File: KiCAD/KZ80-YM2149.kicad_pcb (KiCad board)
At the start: 2 copper layers, 100 x 74 mm, 27 parts, among them J1 ADDR JP, J2 Conn_01x02, J3 SBC8080 BUS, U1 74HC00, U2 74HC138, U3 74HC02, U4 74HC74, U5 YM2149, Y1 3.57MHz

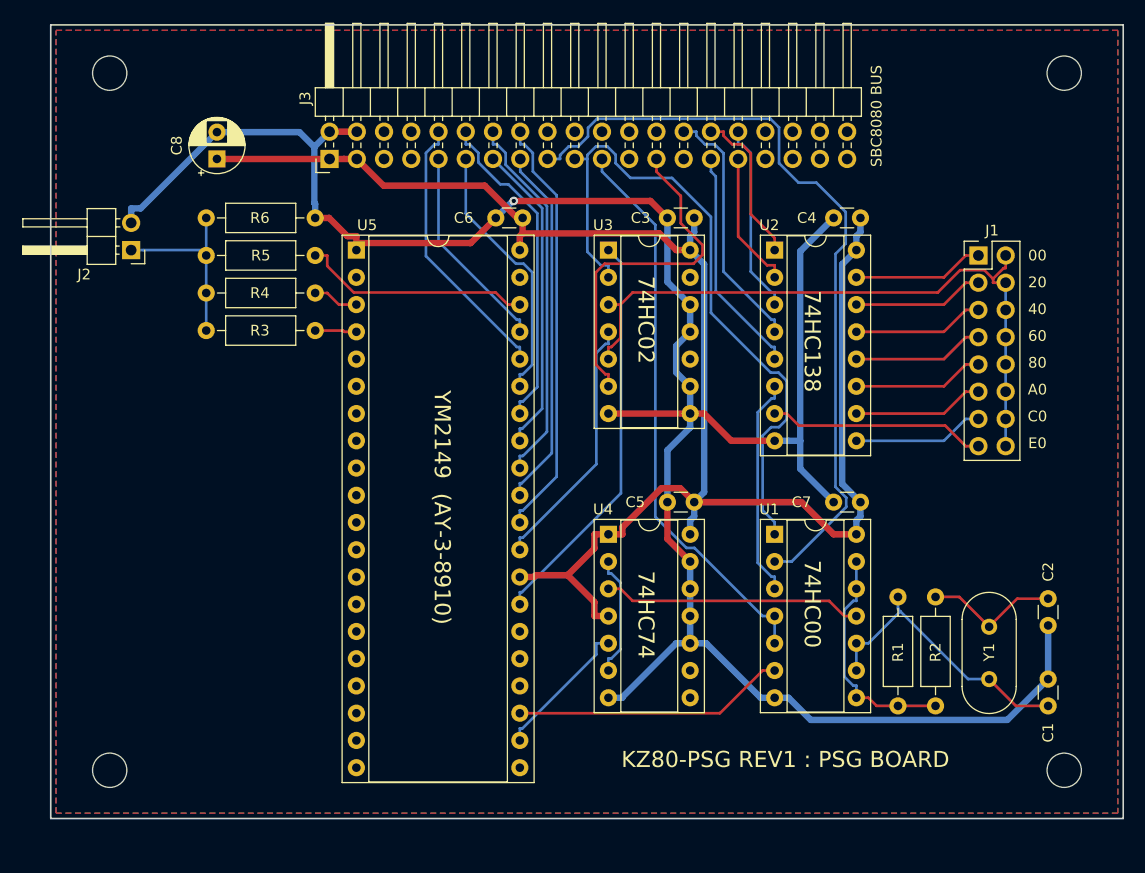
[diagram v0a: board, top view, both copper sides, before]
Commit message: ジョイスティックポート接続&プリントパターン見直し
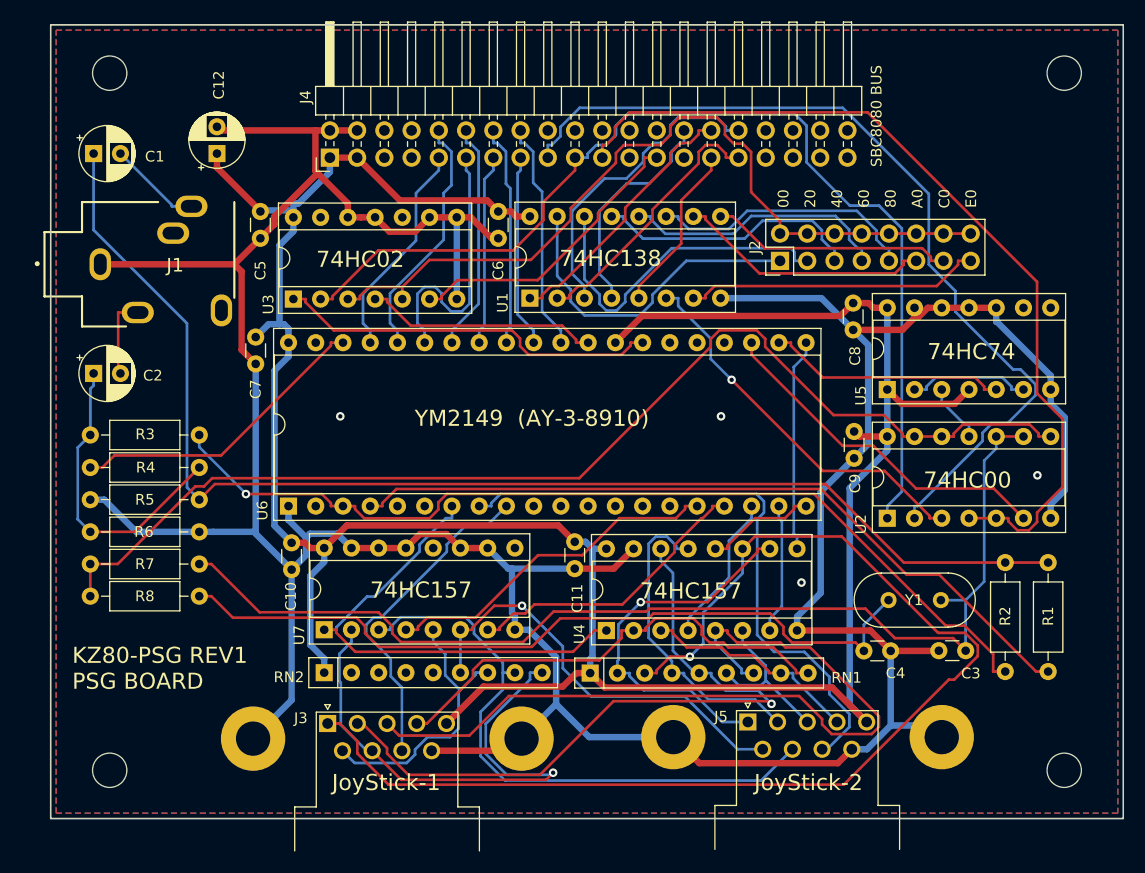
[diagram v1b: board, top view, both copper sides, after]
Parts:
- added C10: 0.1u, Capacitor_THT:C_Disc_D3.0mm_W1.6mm_P2.50mm, F.Cu at (112.5, 98.3)
- added C11: 0.1u, Capacitor_THT:C_Disc_D3.0mm_W1.6mm_P2.50mm, F.Cu at (138.9, 98.2)
- added C12: 10u, Capacitor_THT:CP_Radial_D5.0mm_P2.50mm, F.Cu at (105.5, 62.0)
- added C9: 0.1u, Capacitor_THT:C_Disc_D3.0mm_W1.6mm_P2.50mm, F.Cu at (164.9, 87.9)
- added J4: SBC8080 BUS, Connector_PinHeader_2.54mm:PinHeader_2x20_P2.54mm_Horizontal, F.Cu at (116.0, 62.4)
- added J5: JOYSTICK2, DSUB:DSUB-9_Male_Horizontal_P2.77x2.54mm_EdgePinOffset9.40mm, F.Cu at (155.0, 115.0)
- added R7: 1M, Resistor_THT:R_Axial_DIN0207_L6.3mm_D2.5mm_P10.16mm_Horizontal, F.Cu at (93.7, 100.3)
- added R8: 1k, Resistor_THT:R_Axial_DIN0207_L6.3mm_D2.5mm_P10.16mm_Horizontal, F.Cu at (93.7, 103.3)
- added RN1: 10k, Resistor_THT:R_Array_SIP9, F.Cu at (140.3, 110.4)
- added RN2: 10k, Resistor_THT:R_Array_SIP9, F.Cu at (115.5, 110.4)
- added U6: YM2149, Package_DIP:DIP-40_W15.24mm_Socket, F.Cu at (112.2, 94.9)
- added U7: 74HC157, Package_DIP:DIP-16_W7.62mm_Socket, F.Cu at (115.5, 106.4)
- C1, C2: value 22p -> 1u; footprint Capacitor_THT:C_Disc_D3.0mm_W1.6mm_P2.50mm -> Capacitor_THT:CP_Radial_D5.0mm_P2.50mm
- C3, C4: value 0.1u -> 22p
- C8: value 10u -> 0.1u; footprint Capacitor_THT:CP_Radial_D5.0mm_P2.50mm -> Capacitor_THT:C_Disc_D3.0mm_W1.6mm_P2.50mm
- J1: value ADDR JP -> Audio-Jack-3_2Switches; footprint Connector_PinHeader_2.54mm:PinHeader_2x08_P2.54mm_Vertical -> AJ-1780:AJ-1780
- J2: value Conn_01x02 -> ADDR JP; footprint Connector_PinHeader_2.54mm:PinHeader_1x02_P2.54mm_Horizontal -> Connector_PinHeader_2.54mm:PinHeader_2x08_P2.54mm_Vertical
- J3: value SBC8080 BUS -> JOYSTICK1; footprint Connector_PinHeader_2.54mm:PinHeader_2x20_P2.54mm_Horizontal -> DSUB:DSUB-9_Male_Horizontal_P2.77x2.54mm_EdgePinOffset9.40mm
- R1: value 1M -> 1k
- R2, R3, R5: value 1k -> 2.2k
- R6: value 2k -> 2.2k
- U1: value 74HC00 -> 74HC138; footprint Package_DIP:DIP-14_W7.62mm_Socket -> Package_DIP:DIP-16_W7.62mm_Socket
- U2: value 74HC138 -> 74HC00; footprint Package_DIP:DIP-16_W7.62mm_Socket -> Package_DIP:DIP-14_W7.62mm_Socket
- U4: value 74HC74 -> 74HC157; footprint Package_DIP:DIP-14_W7.62mm_Socket -> Package_DIP:DIP-16_W7.62mm_Socket
- U5: value YM2149 -> 74HC74; footprint Package_DIP:DIP-40_W15.24mm_Socket -> Package_DIP:DIP-14_W7.62mm_Socket
- moved C1 102.8 mm to (94.0, 62.0), turned to 0 degrees
- moved C2 91.4 mm to (94.0, 82.5), turned to 0 degrees
- moved J1 83.6 mm to (92.9, 72.3)
- moved C8 60.8 mm to (164.8, 75.9), turned to 270 degrees
- moved J2 60.5 mm to (158.0, 72.0), turned to 90 degrees
- moved C7 58.5 mm to (109.1, 79.1), turned to 270 degrees
- moved J3 52.6 mm to (115.8, 115.1), turned to 0 degrees
- moved U5 51.2 mm to (168.0, 84.0), turned to 90 degrees
- moved C5 48.7 mm to (109.5, 67.4), turned to 270 degrees
- moved C3 47.6 mm to (175.3, 108.3)
- moved C4 40.4 mm to (165.8, 108.4), turned to 0 degrees
- moved U1 31.7 mm to (134.7, 75.5), turned to 90 degrees
- moved R6 31.2 mm to (93.7, 97.3)
- moved U3 29.7 mm to (112.6, 75.6), turned to 90 degrees
- moved U2 27.1 mm to (168.0, 96.0), turned to 90 degrees
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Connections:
- C1 pad 2: GND -> Net-(C1-Pad2)
- C2 pad 2: GND -> Net-(C2-Pad2)
- C3 pad 1: VCC -> Net-(C3-Pad1)
- C4 pad 1: VCC -> Net-(C4-Pad1)
- J1 pad 1: Net-(J1-Pad1) -> GND
- J1 pad 2: Net-(J1-Pad10) -> Net-(C1-Pad2)
- J1 pad 3: Net-(J1-Pad3) -> (no net)
- J1 pad 4: Net-(J1-Pad10) -> (no net)
- J1 pad 5: Net-(J1-Pad5) -> Net-(C2-Pad2)
- J2 pad 2: GND -> Net-(J2-Pad10)
- J3 pad 1: VCC -> Net-(J3-Pad1)
- J3 pad 2: GND -> Net-(J3-Pad2)
- J3 pad 3: VCC -> Net-(J3-Pad3)
- J3 pad 4: GND -> Net-(J3-Pad4)
- J3 pad 5: Net-(J3-Pad5) -> VCC
- J3 pad 9: D0 -> GND
- R1 pad 1: Net-(R1-Pad1) -> Net-(C1-Pad1)
- R1 pad 2: Net-(C1-Pad1) -> Net-(R1-Pad2)
- R2 pad 1: Net-(R1-Pad1) -> Net-(C1-Pad1)
- R2 pad 2: Net-(C2-Pad1) -> Net-(R2-Pad2)
- R3 pad 1: Net-(J2-Pad1) -> Net-(C2-Pad1)
- R3 pad 2: Net-(R3-Pad2) -> Net-(R2-Pad2)
- R4 pad 1: Net-(J2-Pad1) -> Net-(C2-Pad1)
- R5 pad 1: Net-(J2-Pad1) -> Net-(C1-Pad1)
- R5 pad 2: Net-(R5-Pad2) -> GND
- R6 pad 1: Net-(J2-Pad1) -> Net-(C2-Pad1)
- U1 pad 1: /~IOWR -> /A5
- U1 pad 10: Net-(C1-Pad1) -> Net-(J2-Pad11)
- U1 pad 11: Net-(U1-Pad11) -> Net-(J2-Pad9)
- U1 pad 12: Net-(R1-Pad1) -> Net-(J2-Pad7)
- U1 pad 13: Net-(R1-Pad1) -> Net-(J2-Pad5)
- U1 pad 14: VCC -> Net-(J2-Pad3)
- U1 pad 2: /~IORD -> /A6
- U1 pad 3: Net-(U1-Pad3) -> /A7
- U1 pad 4: /RES -> /A3
- U1 pad 5: /RES -> /A4
- U1 pad 7: GND -> Net-(J2-Pad15)
- U1 pad 8: Net-(R1-Pad1) -> GND
- U1 pad 9: Net-(C1-Pad1) -> Net-(J2-Pad13)
- U2 pad 1: /A5 -> /~IOWR
- U2 pad 10: Net-(J1-Pad11) -> Net-(C3-Pad1)
- U2 pad 11: Net-(J1-Pad9) -> Net-(U2-Pad11)
- U2 pad 12: Net-(J1-Pad7) -> Net-(R7-Pad1)
- U2 pad 13: Net-(J1-Pad5) -> Net-(R7-Pad1)
- U2 pad 14: Net-(J1-Pad3) -> VCC
- U2 pad 2: /A6 -> /~IORD
- U2 pad 3: /A7 -> Net-(U1-Pad6)
- U2 pad 4: /A3 -> /RES
- U2 pad 5: /A4 -> /RES
- U2 pad 6: Net-(U1-Pad3) -> Net-(U2-Pad6)
- U2 pad 7: Net-(J1-Pad15) -> GND
- U2 pad 8: GND -> Net-(R7-Pad1)
- U2 pad 9: Net-(J1-Pad13) -> Net-(C3-Pad1)
- U3 pad 10: Net-(U3-Pad10) -> (no net)
- U3 pad 13: Net-(U3-Pad13) -> (no net)
- U3 pad 3: Net-(J1-Pad10) -> Net-(J2-Pad10)
- U3 pad 5: Net-(J1-Pad10) -> Net-(J2-Pad10)
- U4 pad 1: VCC -> Net-(U4-Pad1)
- U4 pad 10: GND -> Net-(J5-Pad1)
- U4 pad 11: GND -> Net-(J3-Pad1)
- U4 pad 12: GND -> Net-(U4-Pad12)
- U4 pad 13: GND -> Net-(J5-Pad2)
- U4 pad 14: VCC -> Net-(J3-Pad2)
- U4 pad 2: Net-(U4-Pad2) -> Net-(J3-Pad4)
- U4 pad 3: Net-(U1-Pad11) -> Net-(J5-Pad4)
- U4 pad 4: VCC -> Net-(U4-Pad4)
- U4 pad 5: Net-(U4-Pad5) -> Net-(J3-Pad3)
- U4 pad 6: Net-(U4-Pad2) -> Net-(J5-Pad3)
- U4 pad 7: GND -> Net-(U4-Pad7)
- U4 pad 8: Net-(U4-Pad8) -> GND
- U5 pad 1: GND -> VCC
- U5 pad 10: Net-(U5-Pad10) -> GND
- U5 pad 11: Net-(U5-Pad11) -> GND
- U5 pad 12: Net-(U5-Pad12) -> GND
- U5 pad 13: Net-(U5-Pad13) -> GND
- U5 pad 14: Net-(U5-Pad14) -> VCC
- U5 pad 2: (no net) -> Net-(U5-Pad2)
- U5 pad 3: Net-(R4-Pad2) -> Net-(U2-Pad11)
- U5 pad 4: Net-(R3-Pad2) -> VCC
- U5 pad 5: (no net) -> Net-(U5-Pad5)
- U5 pad 6: Net-(U5-Pad6) -> Net-(U5-Pad2)
- U5 pad 7: Net-(U5-Pad7) -> GND
- U5 pad 8: Net-(U5-Pad8) -> (no net)
- U5 pad 9: Net-(U5-Pad9) -> (no net)
- Y1 pad 1: Net-(C1-Pad1) -> Net-(C3-Pad1)
- Y1 pad 2: Net-(C2-Pad1) -> Net-(C4-Pad1)
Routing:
- net GND: track 214.3 -> 348.5 mm, vias 1 -> 4
- net Net-(J3-Pad1): track 0.00 -> 113.3 mm, vias 0 -> 1
- net Net-(R7-Pad1): track 0.00 -> 108.0 mm
- net Net-(C3-Pad1): track 0.00 -> 103.8 mm
- net VCC: track 155.8 -> 252.3 mm
- net Net-(C1-Pad1): track 27.0 -> 119.1 mm
- net Net-(R2-Pad2): track 0.00 -> 88.5 mm, vias 0 -> 1
- net Net-(J2-Pad10): track 0.00 -> 75.9 mm
- net Net-(J3-Pad3): track 0.00 -> 75.7 mm
- net Net-(C4-Pad1): track 0.00 -> 73.1 mm
- net Net-(R1-Pad2): track 0.00 -> 71.1 mm
- net Net-(J3-Pad2): track 0.00 -> 65.2 mm, vias 0 -> 1
- net Net-(J1-Pad10): track 62.8 -> 0.00 mm
- net Net-(J5-Pad8): track 0.00 -> 57.4 mm
- net Net-(J5-Pad7): track 0.00 -> 56.3 mm
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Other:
- board text added: "74HC157"
- board text added: "JoyStick-1"
- board text added: "JoyStick-2"
- board text added: "KZ80-PSG REV1 PSG BOARD"
- board text removed: "KZ80-PSG REV1 : PSG BOARD"

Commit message: パターン間違い修正&ガーバーデータ再出力
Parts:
- moved R7 90.5 mm to (183.6, 110.7), turned to 90 degrees
- moved R1 88.4 mm to (95.4, 88.6), turned to 0 degrees
- moved R8 86.9 mm to (180.2, 110.7), turned to 90 degrees
- moved R2 84.0 mm to (95.4, 91.7), turned to 0 degrees
- moved R3 6.77 mm to (95.4, 94.8)
- moved R4 6.77 mm to (105.6, 97.8)
- moved R5 6.77 mm to (105.6, 100.8)
- moved R6 6.77 mm to (95.4, 103.8)
- moved J1 1.24 mm to (91.7, 72.3)
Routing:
- net Net-(C1-Pad1): track 119.1 -> 44.2 mm
- net Net-(R2-Pad2): track 88.5 -> 15.9 mm, vias 1 -> 0
- net Net-(C3-Pad1): track 103.8 -> 32.7 mm
- net Net-(R7-Pad1): track 108.0 -> 40.9 mm
- net Net-(J3-Pad1): track 113.3 -> 51.5 mm, vias 1 -> 0
- net Net-(R1-Pad2): track 71.1 -> 17.0 mm
- net Net-(C4-Pad1): track 73.1 -> 19.1 mm
- net Net-(J2-Pad5): track 25.2 -> 52.6 mm
- net Net-(J3-Pad3): track 75.7 -> 51.9 mm
- net Net-(J2-Pad3): track 32.1 -> 46.2 mm
- net Net-(J3-Pad2): track 65.2 -> 55.3 mm, vias 1 -> 0
- net Net-(J2-Pad7): track 25.3 -> 34.0 mm
- net Net-(J2-Pad13): track 22.7 -> 30.6 mm
- net Net-(J5-Pad6): track 40.0 -> 47.8 mm, vias 1 -> 0
- net Net-(R4-Pad2): track 28.5 -> 35.0 mm
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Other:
- board text added: "KZ80-PSG REV1 PSG & JOYSTICK BOARD"
- board text removed: "KZ80-PSG REV1 PSG BOARD"
